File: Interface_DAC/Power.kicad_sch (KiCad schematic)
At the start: 41 parts, among them Q1 AO3401, U10 TPS7A3301RGW, U7 TPS62A02ADRL, U8 TPS65131RGE, U9 TPS7A4701xRGW

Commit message: Schematic Tinkering and PCB Layout
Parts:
- renumbered C50 to C58, C51 to C59, C52 to C60, C53 to C61, C54 to C62, C55 to C63, C56 to C64, C57 to C65, C58 to C66, C59 to C67, C60 to C68, C61 to C69, C62 to C70, C63 to C71, C64 to C72, C65 to C73, C66 to C74, C67 to C75, C68 to C76, C69 to C77, R9 to R22, R10 to R23, R11 to R24, R12 to R25, R13 to R26, R14 to R27, R15 to R28, R16 to R29, R17 to R30, R18 to R31, R19 to R32, U7 to U10, U8 to U11, U9 to U12, U10 to U13

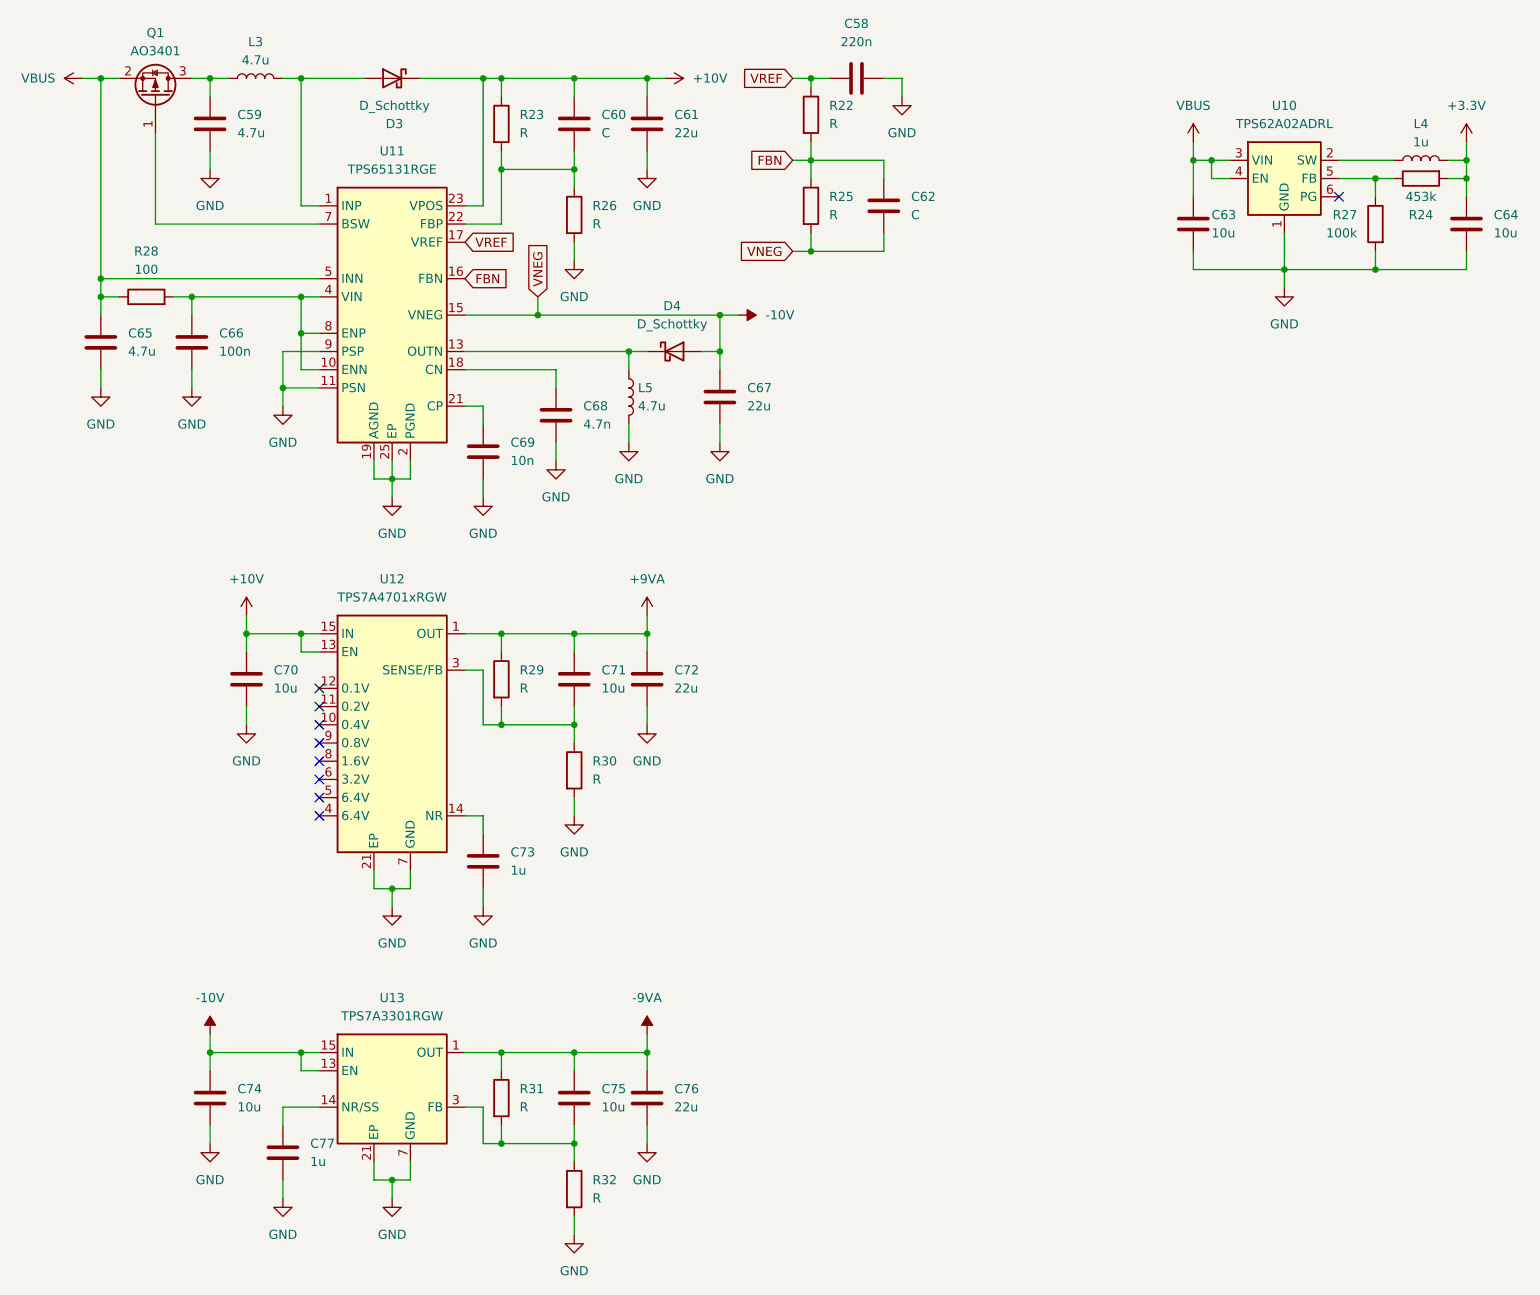
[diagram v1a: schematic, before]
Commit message: Schematic Design and Library Relink
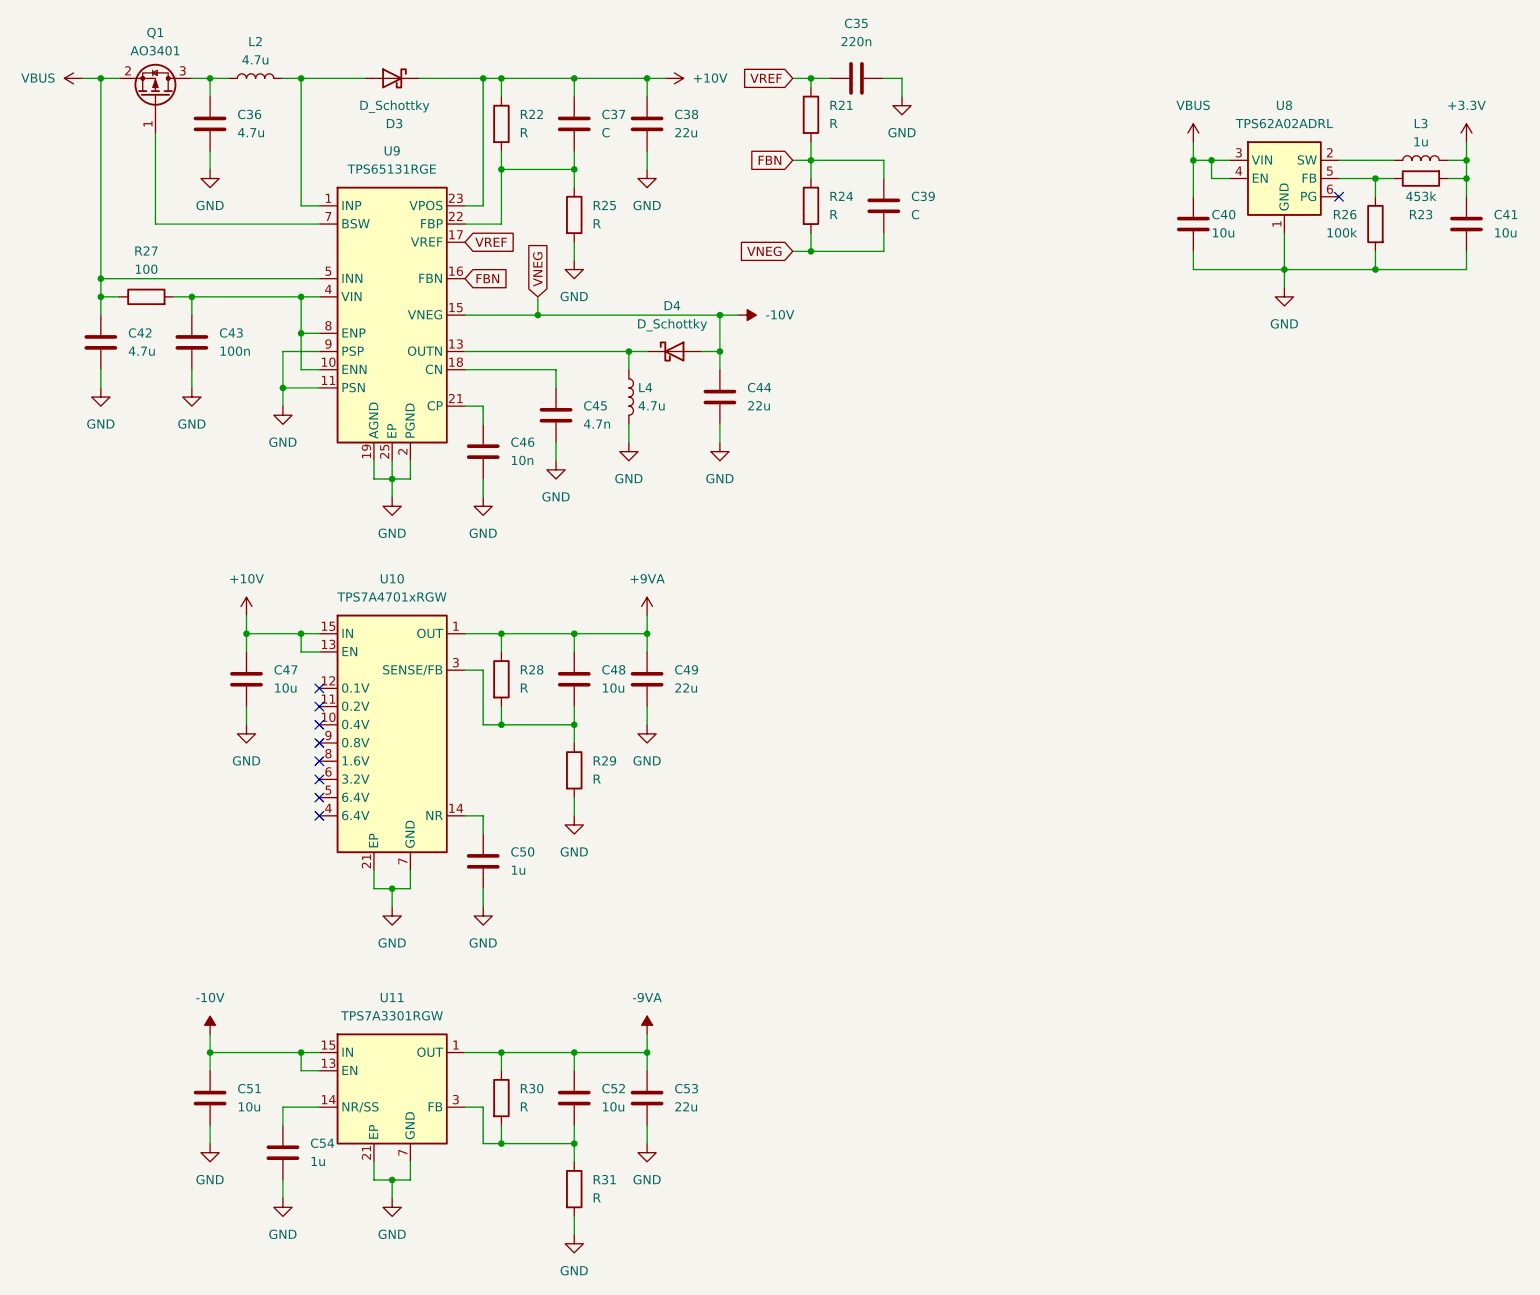
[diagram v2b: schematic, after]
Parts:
- renumbered C58 to C35, C59 to C36, C60 to C37, C61 to C38, C62 to C39, C63 to C40, C64 to C41, C65 to C42, C66 to C43, C67 to C44, C68 to C45, C69 to C46, C70 to C47, C71 to C48, C72 to C49, C73 to C50, C74 to C51, C75 to C52, C76 to C53, C77 to C54, L3 to L2, L4 to L3, L5 to L4, R22 to R21, R23 to R22, R24 to R23, R25 to R24, R26 to R25, R27 to R26, R28 to R27, R29 to R28, R30 to R29, R31 to R30, R32 to R31, U12 to U10, U13 to U11, U10 to U8, U11 to U9

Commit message: Schematic Design
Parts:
- renumbered C35 to C41, C36 to C42, C37 to C43, C38 to C44, C39 to C45, C40 to C46, C41 to C47, C42 to C48, C43 to C49, C44 to C50, C45 to C51, C46 to C52, C47 to C53, C48 to C54, C49 to C55, C50 to C56, C51 to C57, C52 to C58, C53 to C59, C54 to C60, R21 to R25, R22 to R26, R23 to R27, R24 to R28, R25 to R29, R26 to R30, R27 to R31, R28 to R32, R29 to R33, R30 to R34, R31 to R35, U9 to U10, U10 to U11, U11 to U12, U8 to U9
